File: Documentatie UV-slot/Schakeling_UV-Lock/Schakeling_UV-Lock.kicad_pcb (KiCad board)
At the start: 2 copper layers, 7.6 x 1.2 mm, 21 parts, among them Q1 BC817

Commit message: Veel nieuwe aanpassing in de Kicad files ( en ook een paar in de code)
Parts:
- removed UART_Suikertje1: 282841-2, components:TE_282841-2
- added UART_pins1: Conn_01x04_Female, Connector_PinSocket_2.54mm:PinSocket_1x04_P2.54mm_Vertical, F.Cu at (119.5, 80.2)
- C2: footprint Capacitor_SMD:C_0805_2012Metric_Pad1.18x1.45mm_HandSolder -> Capacitor_SMD:CP_Elec_6.3x7.7
- moved C4 14.5 mm to (90.1, 83.2)
- moved C2 9.49 mm to (90.1, 77.4)
- moved MicroUSB_Poort1 8.01 mm to (70.2, 78.6), turned to -90 degrees
- moved LDO1 6.09 mm to (80.8, 76.5), turned to 0 degrees
- moved C3 3.40 mm to (86.9, 84.1)
- moved R1 2.35 mm to (85.4, 87.0)
- moved C1 0.78 mm to (81.6, 86.5)
- moved ENABLE1 0.71 mm to (75.8, 86.3)
- renumbered LCD_Suikertje1 to 282841-1
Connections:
- ESP_eindpuzzel1 pad 34: Net-(ESP_eindpuzzel1-Pad34) -> RX
- ESP_eindpuzzel1 pad 35: Net-(ESP_eindpuzzel1-Pad35) -> TX
- UV-Lamp_Relay1 pad COM: unconnected-(UV-Lamp_Relay1-PadCOM) -> Net-(UV-Lamp_Relay1-PadCOM)
- UV-Lamp_Relay1 pad NC: Net-(UV-Lamp_Relay1-PadNC) -> unconnected-(UV-Lamp_Relay1-PadNC)
- UV-lamp_Suikertje1 pad 2: Net-(UV-Lamp_Relay1-PadNC) -> Net-(UV-Lamp_Relay1-PadCOM)
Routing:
- net GND: track 116.2 -> 152.1 mm, vias 1 -> 4
- net 5V: track 103.7 -> 74.9 mm, vias 4 -> 2
- net 3.3V: track 53.0 -> 81.2 mm, vias 3 -> 4
- net Net-(UV-Lamp_Relay1-PadNC): track 28.0 -> 0.00 mm
- net Net-(ESP_eindpuzzel1-Pad35): track 15.3 -> 0.00 mm, vias 1 -> 0
- net Net-(UV-Lamp_Relay1-PadCOM): track 0.00 -> 14.2 mm
- net Net-(ESP_eindpuzzel1-Pad34): track 14.0 -> 0.00 mm, vias 1 -> 0
- net TX: track 0.00 -> 8.94 mm, vias 0 -> 1
- net RX: track 0.00 -> 7.95 mm, vias 0 -> 1
- net unconnected-(MicroUSB_Poort1-Pad6): track 6.75 -> 0.00 mm
- net IO2: track 35.2 -> 36.3 mm
- added copper zone on B.Cu, net GND
- added copper zone on F.Cu, net GND
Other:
- board size 7.6 x 1.2 mm -> 56.2 x 61 mm
- board text added: "UV-Slot"
- board text added: "UV-slot"

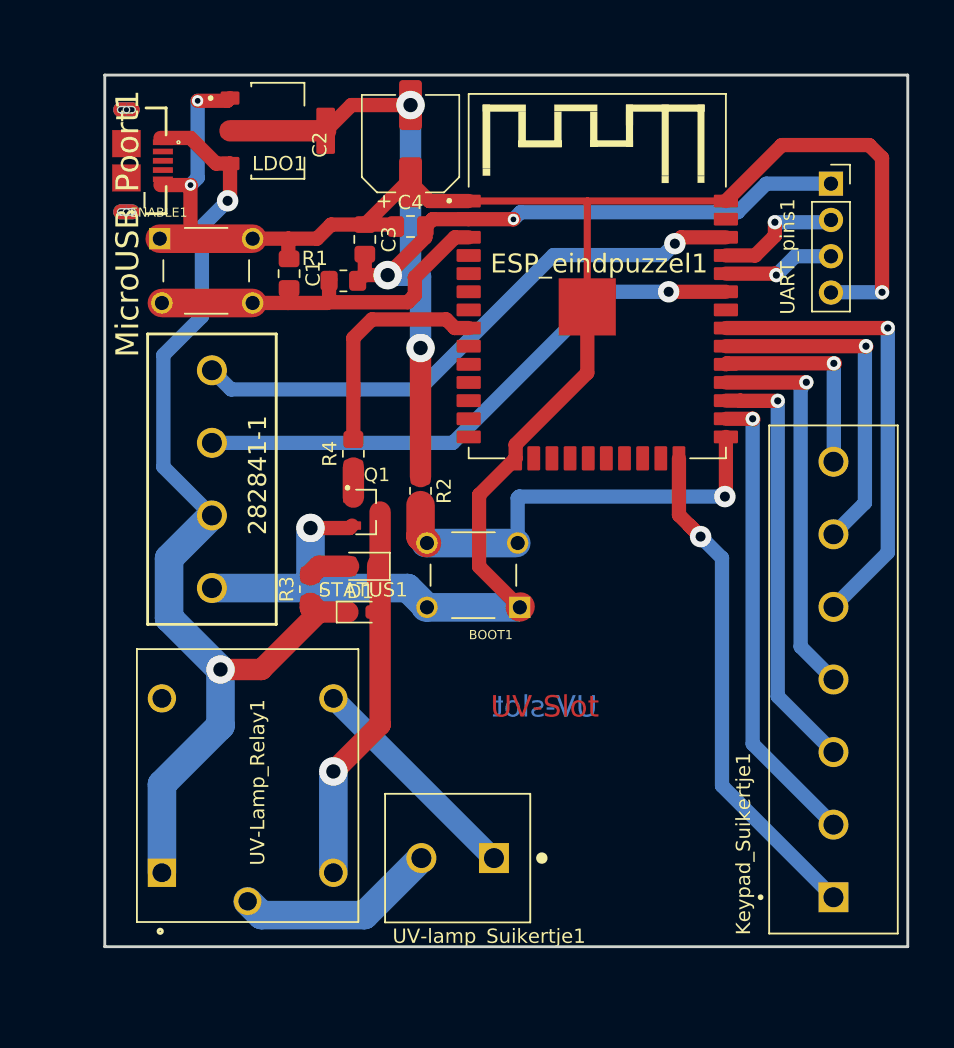
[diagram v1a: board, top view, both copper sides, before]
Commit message: Wifi antennes extra ruimte gegeven
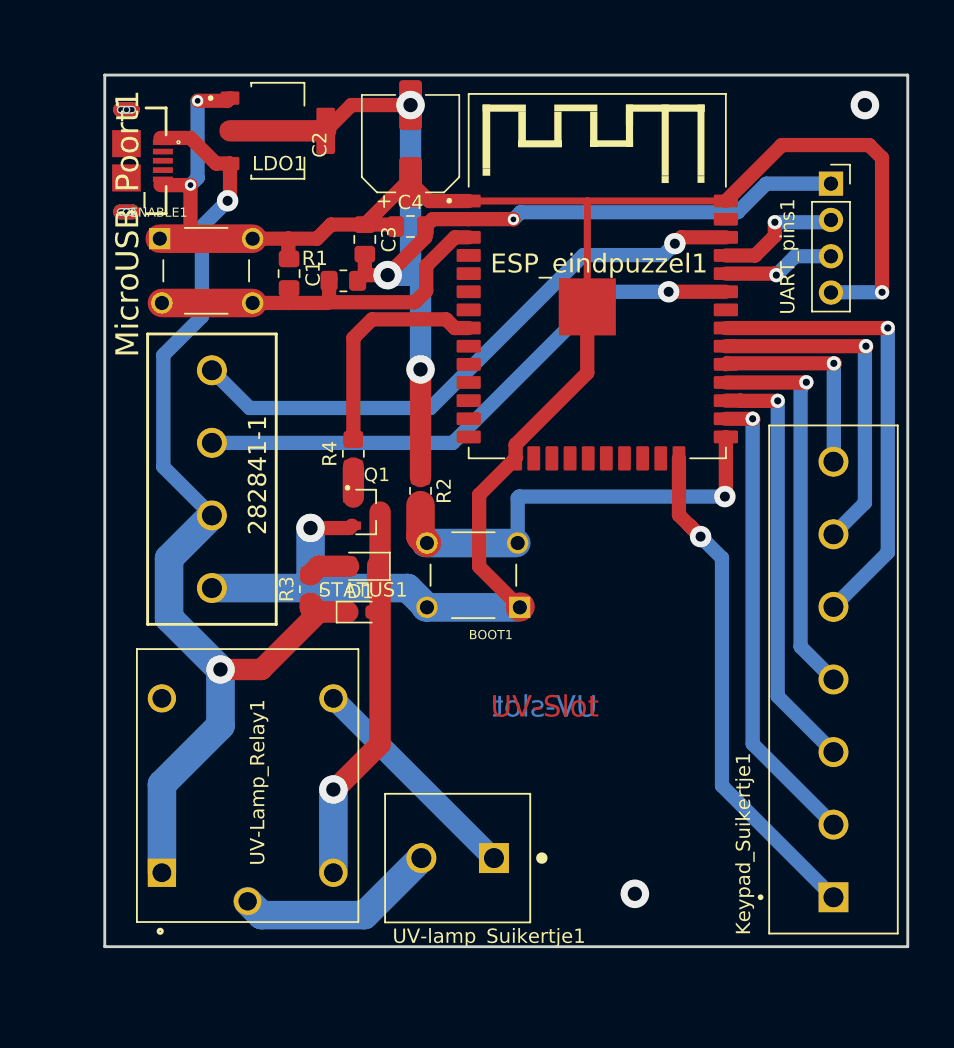
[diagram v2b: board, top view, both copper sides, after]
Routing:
- net IO22: track 40.9 -> 42.0 mm
- net 3.3V: track 81.2 -> 81.7 mm
- net GND: vias 4 -> 6
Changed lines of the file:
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@@
   (via (at 83.1 104.3) (size 2) (drill 1) (layers "F.Cu" "B.Cu") (net 1))
   (via (at 75.2 74.4) (size 0.8) (drill 0.4) (layers "F.Cu" "B.Cu") (net 1))
+  (via (at 121.9 74.7) (size 2) (drill 1) (layers "F.Cu" "B.Cu") (free) (net 1))
   (via (at 123.1 87.8) (size 1) (drill 0.5) (layers "F.Cu" "B.Cu") (net 1))
   (via (at 74.7 80.3) (size 0.8) (drill 0.4) (layers "F.Cu" "B.Cu") (net 1))
+  (via (at 105.8 129.9) (size 2) (drill 1) (layers "F.Cu" "B.Cu") (free) (net 1))
   (segment (start 74.7 80.3) (end 75.2 79.8) (width 1) (layer "B.Cu") (net 1))
   (segment (start 89.9 108.5) (end 83.1 108.5) (width 2) (layer "B.Cu") (net 1))
@@
   (segment (start 112.1 102.1) (end 97.7 102.1) (width 1) (layer "B.Cu") (net 2))
   (segment (start 84.25 88.55) (end 84.3 88.5) (width 1) (layer "F.Cu") (net 3))
-  (segment (start 90.4 88) (end 89.9 88.5) (width 1) (layer "F.Cu") (net 3))
+  (segment (start 91.2 87.7) (end 90.4 88.5) (width 1) (layer "F.Cu") (net 3))
+  (segment (start 93.203451 83.955) (end 91.2 85.958451) (width 1) (layer "F.Cu") (net 3))
+  (segment (start 90.4 88.5) (end 84.3 88.5) (width 1) (layer "F.Cu") (net 3))
+  (segment (start 81.55 88.55) (end 84.25 88.55) (width 1) (layer "F.Cu") (net 3))
+  (segment (start 84.4 86.8) (end 84.4 88.4) (width 1) (layer "F.Cu") (net 3))
+  (segment (start 91.2 85.958451) (end 91.2 87.7) (width 1) (layer "F.Cu") (net 3))
+  (segment (start 81.55 87.5875) (end 81.6 87.5375) (width 1) (layer "F.Cu") (net 3))
   (segment (start 94.17 83.955) (end 93.203451 83.955) (width 1) (layer "F.Cu") (net 3))
-  (segment (start 81.55 88.55) (end 84.25 88.55) (width 1) (layer "F.Cu") (net 3))
-  (segment (start 93.203451 83.955) (end 90.4 86.758451) (width 1) (layer "F.Cu") (net 3))
-  (segment (start 84.4 86.8) (end 84.4 88.4) (width 1) (layer "F.Cu") (net 3))
-  (segment (start 81.55 87.5875) (end 81.6 87.5375) (width 1) (layer "F.Cu") (net 3))
-  (segment (start 90.4 86.758451) (end 90.4 88) (width 1) (layer "F.Cu") (net 3))
   (segment (start 79.05 88.55) (end 81.55 88.55) (width 1) (layer "F.Cu") (net 3))
   (segment (start 81.55 88.55) (end 81.55 87.5875) (width 1) (layer "F.Cu") (net 3))
   (segment (start 84.4 86.8) (end 84.5 86.9) (width 1) (layer "F.Cu") (net 3))
   (segment (start 84.4 88.4) (end 84.3 88.5) (width 1) (layer "F.Cu") (net 3))
-  (segment (start 89.9 88.5) (end 84.3 88.5) (width 1) (layer "F.Cu") (net 3))
   (segment (start 79.05 88.55) (end 72.7 88.55) (width 2) (layer "F.Cu") (net 3))
   (segment (start 91.1375 83.2) (end 91.1375 83.9625) (width 1) (layer "F.Cu") (net 4))
@@
   (segment (start 97.285 82.685) (end 97.3 82.7) (width 1) (layer "F.Cu") (net 4))
   (segment (start 85.959 74.7) (end 84.159 76.5) (width 1) (layer "F.Cu") (net 4))
-  (segment (start 90.8 100.7) (end 90.8 92.2) (width 1.5) (layer "F.Cu") (net 4))
   (segment (start 77.469 76.5) (end 84.159 76.5) (width 1.5) (layer "F.Cu") (net 4))
   (segment (start 89.8 74.7) (end 85.959 74.7) (width 1) (layer "F.Cu") (net 4))
@@
   (segment (start 88.5 86.6) (end 87 86.6) (width 1) (layer "F.Cu") (net 4))
   (segment (start 91.1375 83.9625) (end 88.5 86.6) (width 1) (layer "F.Cu") (net 4))
+  (segment (start 90.8 93.2) (end 90.8 100.7) (width 1.5) (layer "F.Cu") (net 4))
   (segment (start 86.9 85.1375) (end 86.9 86.5) (width 1) (layer "F.Cu") (net 4))
   (segment (start 86.9 86.5) (end 86.4 87) (width 1) (layer "F.Cu") (net 4))
@@
   (via (at 90.1 74.7) (size 2) (drill 1) (layers "F.Cu" "B.Cu") (net 4))
   (via (at 97.3 82.7) (size 0.8) (drill 0.4) (layers "F.Cu" "B.Cu") (net 4))
-  (via (at 90.8 91.7) (size 2) (drill 1) (layers "F.Cu" "B.Cu") (free) (net 4))
+  (via (at 90.8 93.2) (size 2) (drill 1) (layers "F.Cu" "B.Cu") (free) (net 4))
   (segment (start 115 80.2) (end 119.525 80.2) (width 1) (layer "B.Cu") (net 4))
+  (segment (start 90.7 86.6) (end 88.5 86.6) (width 1.5) (layer "B.Cu") (net 4))
   (segment (start 90.1 86.4) (end 90.2 86.5) (width 1.5) (layer "B.Cu") (net 4))
   (segment (start 97.8 82.2) (end 113 82.2) (width 1) (layer "B.Cu") (net 4))
   (segment (start 90.1 74.7) (end 90.1 86.4) (width 1.5) (layer "B.Cu") (net 4))
   (segment (start 90.2 86.5) (end 90.1 86.6) (width 1.5) (layer "B.Cu") (net 4))
-  (segment (start 88.5 86.6) (end 90.7 86.6) (width 1.5) (layer "B.Cu") (net 4))
   (segment (start 90.1 86.6) (end 88.5 86.6) (width 1.5) (layer "B.Cu") (net 4))
-  (segment (start 90.8 86.7) (end 90.8 91.7) (width 1.5) (layer "B.Cu") (net 4))
+  (segment (start 90.8 86.7) (end 90.7 86.6) (width 1.5) (layer "B.Cu") (net 4))
   (segment (start 97.3 82.7) (end 97.8 82.2) (width 1) (layer "B.Cu") (net 4))
-  (segment (start 90.7 86.6) (end 90.8 86.7) (width 1.5) (layer "B.Cu") (net 4))
+  (segment (start 90.8 93.2) (end 90.8 86.7) (width 1.5) (layer "B.Cu") (net 4))
   (segment (start 113 82.2) (end 115 80.2) (width 1) (layer "B.Cu") (net 4))
   (segment (start 77.469 78.79) (end 77.469 81.231) (width 1) (layer "F.Cu") (net 5))
@@
   (segment (start 75.5 89.5) (end 72.8 92.2) (width 1) (layer "B.Cu") (net 5))
   (segment (start 75.5 83.2) (end 75.5 89.5) (width 1) (layer "B.Cu") (net 5))
+  (segment (start 84.7 122.6) (end 84.8 122.6) (width 1.5) (layer "F.Cu") (net 6))
+  (segment (start 87.969511 119.430489) (end 87.969511 107.920489) (width 1.5) (layer "F.Cu") (net 6))
+  (segment (start 84.8 122.6) (end 87.969511 119.430489) (width 1.5) (layer "F.Cu") (net 6))
   (segment (start 87.969511 103.179511) (end 87.969511 107.920489) (width 1.5) (layer "F.Cu") (net 6))
   (segment (start 87.8 108.09) (end 87.8 106.91) (width 1.5) (layer "F.Cu") (net 6))
   (segment (start 87.969511 107.920489) (end 87.8 108.09) (width 1.5) (layer "F.Cu") (net 6))
-  (segment (start 84.7 121.33625) (end 87.969511 118.066739) (width 1.5) (layer "F.Cu") (net 6))
-  (segment (start 87.969511 118.066739) (end 87.969511 107.920489) (width 1.5) (layer "F.Cu") (net 6))
-  (via (at 84.7 121.33625) (size 2) (drill 1) (layers "F.Cu" "B.Cu") (net 6))
-  (segment (start 84.7 128.42375) (end 84.7 121.33625) (width 2) (layer "B.Cu") (net 6))
+  (via (at 84.7 122.6) (size 2) (drill 1) (layers "F.Cu" "B.Cu") (net 6))
+  (segment (start 84.7 128.42375) (end 84.7 122.6) (width 2) (layer "B.Cu") (net 6))
   (segment (start 109.045 83.955) (end 112.17 83.955) (width 1) (layer "F.Cu") (net 8))
   (segment (start 108.6 84.4) (end 109.045 83.955) (width 1) (layer "F.Cu") (net 8))
   (via (at 108.6 84.4) (size 1.5) (drill 0.7) (layers "F.Cu" "B.Cu") (net 8))
+  (segment (start 78.84 95.9) (end 76.2 93.26) (width 1) (layer "B.Cu") (net 8))
+  (segment (start 107.8 85.2) (end 102.2 85.2) (width 1) (layer "B.Cu") (net 8))
   (segment (start 108.6 84.4) (end 107.8 85.2) (width 1) (layer "B.Cu") (net 8))
-  (segment (start 107.8 85.2) (end 100.1 85.2) (width 1) (layer "B.Cu") (net 8))
-  (segment (start 100.1 85.2) (end 90.7 94.6) (width 1) (layer "B.Cu") (net 8))
-  (segment (start 77.54 94.6) (end 76.2 93.26) (width 1) (layer "B.Cu") (net 8))
-  (segment (start 90.7 94.6) (end 77.54 94.6) (width 1) (layer "B.Cu") (net 8))
+  (segment (start 102.2 85.2) (end 91.5 95.9) (width 1) (layer "B.Cu") (net 8))
+  (segment (start 91.5 95.9) (end 78.84 95.9) (width 1) (layer "B.Cu") (net 8))
   (segment (start 112.17 87.765) (end 108.165 87.765) (width 1) (layer "F.Cu") (net 9))
   (segment (start 108.165 87.765) (end 108.1 87.7) (width 1) (layer "F.Cu") (net 9))
@@
       )
     )
+  )
+  (zone (net 0) (net_name "") (layers F&B.Cu) (hatch edge 0.508)
+    (connect_pads (clearance 0))
+    (min_thickness 0.254)
+    (keepout (tracks allowed) (vias allowed) (pads allowed ) (copperpour not_allowed) (footprints allowed))
+    (fill (thermal_gap 0.508) (thermal_bridge_width 0.508))
+    (polygon
+      (pts
+        (xy 113.4 81.1)
+        (xy 92.8 81.1)
+        (xy 92.8 72.7)
+        (xy 92.8 81)
+        (xy 92.8 72.6)
+        (xy 113.4 72.6)
+      )
+    )

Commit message: Finale design PCB's
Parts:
- added C5: 0.1u, Capacitor_SMD:C_0805_2012Metric_Pad1.18x1.45mm_HandSolder, F.Cu at (94.4, 102.8)
- added C6: 10u, Capacitor_SMD:C_0805_2012Metric_Pad1.18x1.45mm_HandSolder, F.Cu at (76.3, 76.5)
- moved LDO 1.23 mm to (82.0, 76.5)
- renumbered ENABLE1 to ENABLE, Keypad_Suikertje1 to Keypad, 282841-1 to LCD, LDO1 to LDO, STATUS1 to LED, MicroUSB_Poort1 to MicroUSB, Q1 to NPN, UV-lamp_Suikertje1 to UV-lamp
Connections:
- MicroUSB pad 6: unconnected-(MicroUSB_Poort1-Pad6) -> GND
- MicroUSB pad 7: unconnected-(MicroUSB_Poort1-Pad6) -> GND
- MicroUSB pad 8: unconnected-(MicroUSB_Poort1-Pad6) -> GND
- MicroUSB pad 9: unconnected-(MicroUSB_Poort1-Pad6) -> GND
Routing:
- net GND: track 152.1 -> 164.3 mm
- net Net-(ESP_eindpuzzel1-Pad25): track 31.1 -> 33.7 mm
- net 5V: track 74.9 -> 76.7 mm
- net 3.3V: track 81.7 -> 80.4 mm
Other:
- board text removed: "UV-slot"
